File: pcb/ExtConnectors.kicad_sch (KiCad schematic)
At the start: 15 parts, among them J1 USB_C_Receptacle_USB2.0_14P, U2 TPD6S300ARUKR, U3 AP2112K-3.3

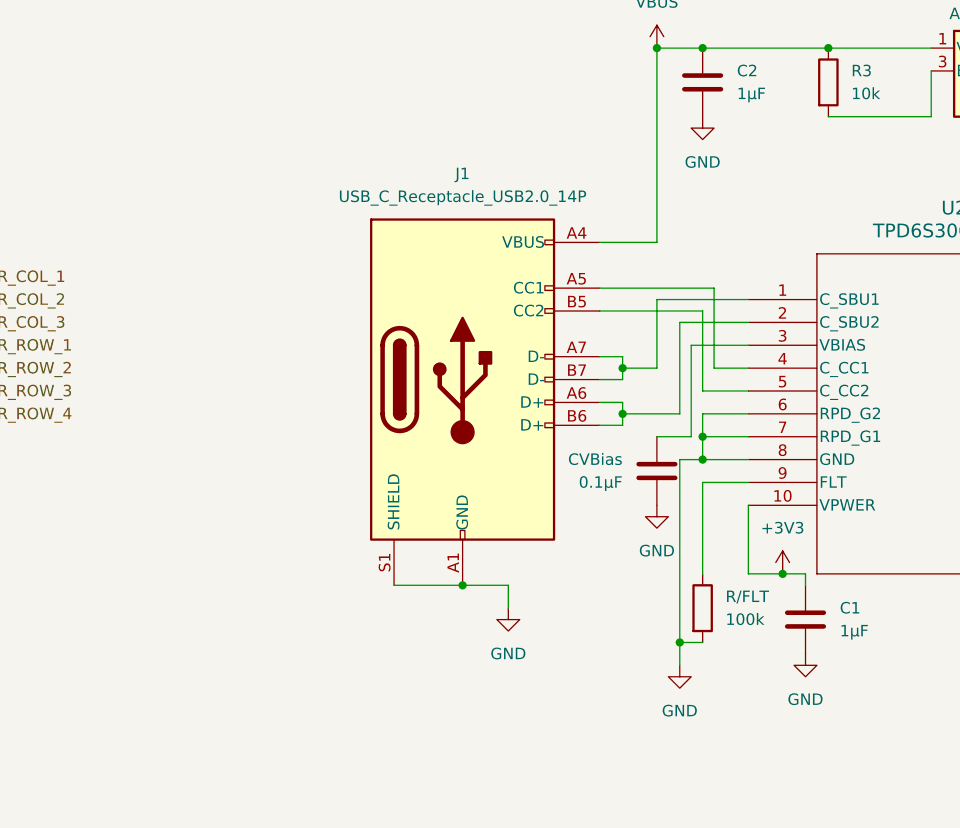
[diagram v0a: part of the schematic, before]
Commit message: First pass of applying footprints to most components.
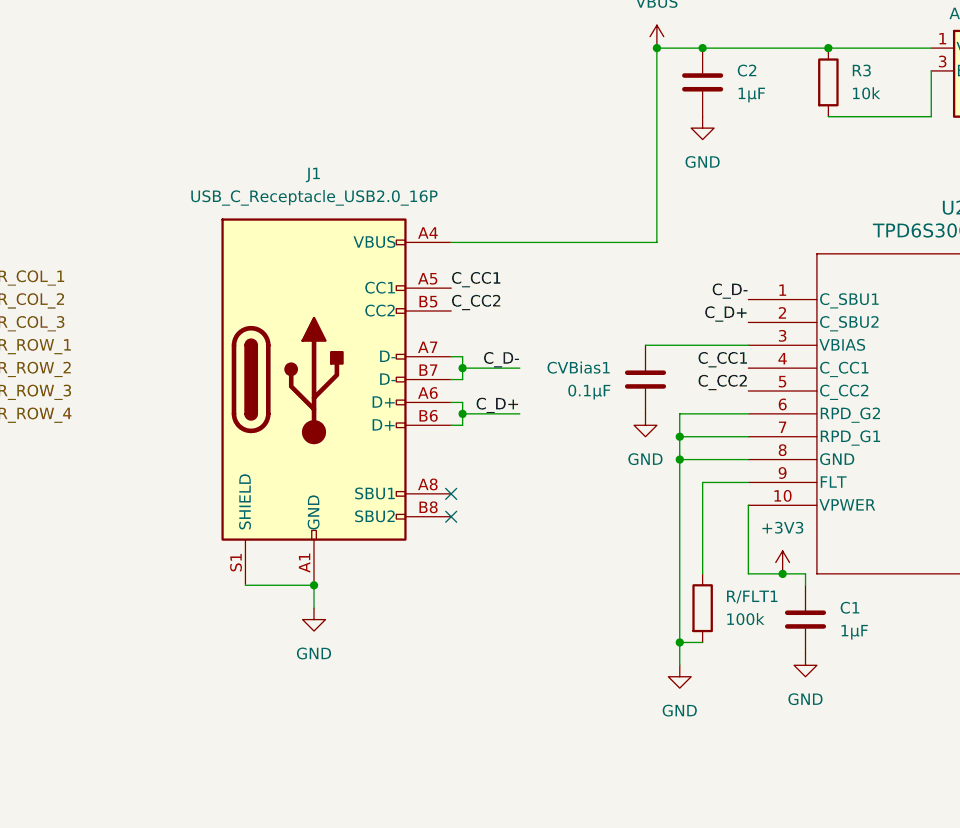
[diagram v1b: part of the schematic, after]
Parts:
- C1, C2, C3: footprint (none) -> Capacitor_SMD:C_0603_1608Metric_Pad1.08x0.95mm_HandSolder
- CVBias1: renamed from CVBias; footprint (none) -> Capacitor_SMD:C_0603_1608Metric_Pad1.08x0.95mm_HandSolder
- J1: value USB_C_Receptacle_USB2.0_14P -> USB_C_Receptacle_USB2.0_16P; symbol Connector:USB_C_Receptacle_USB2.0_14P -> Connector:USB_C_Receptacle_USB2.0_16P
- JP8, JP9: footprint (none) -> Jumper:SolderJumper-3_P1.3mm_Bridged12_RoundedPad1.0x1.5mm_NumberLabels
- R/FLT1: renamed from R/FLT; footprint (none) -> Resistor_SMD:R_0603_1608Metric_Pad0.98x0.95mm_HandSolder
- R1, R2, R3: footprint (none) -> Resistor_SMD:R_0603_1608Metric_Pad0.98x0.95mm_HandSolder
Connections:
- net C_CC1: now reaches J1.A5 (CC1), U2.4 (C_CC1)
- net C_D+: now reaches J1.A6 (D+), J1.B6 (D+), U2.2 (C_SBU2)
- net C_D-: now reaches J1.A7 (D-), J1.B7 (D-), U2.1 (C_SBU1)
- net C_CC2: now reaches J1.B5 (CC2), U2.5 (C_CC2)
- no-connect marks 0 -> 2
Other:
- moved on the sheet: CVBias1

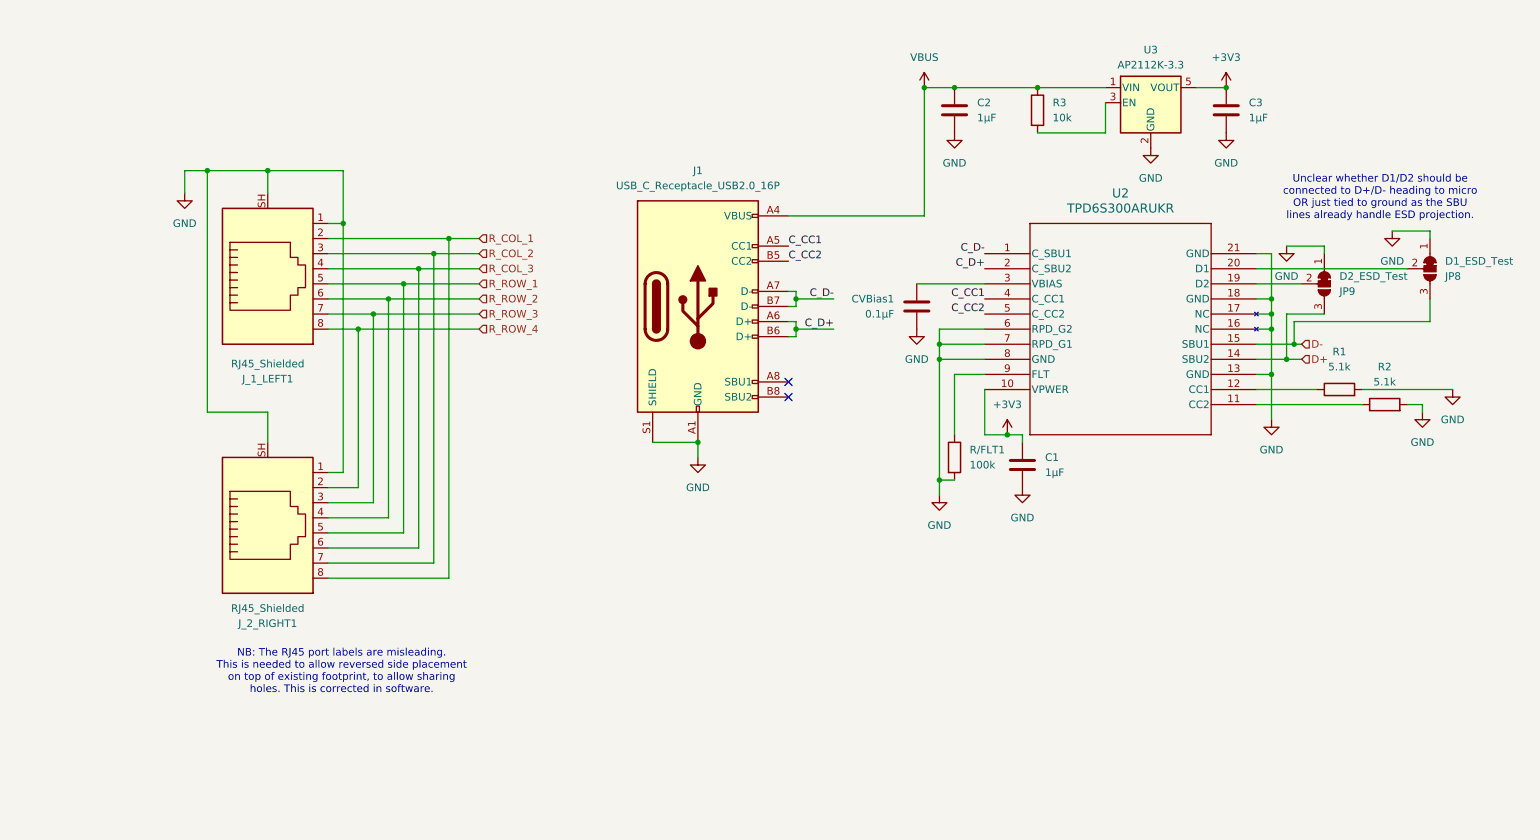
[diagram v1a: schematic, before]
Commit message: Switching from a full USB protection chip for OVP and ESD, needed for USB PD to only ESD protection. Also added chips for ESD protection for the Ethernet connectors to the other hand.
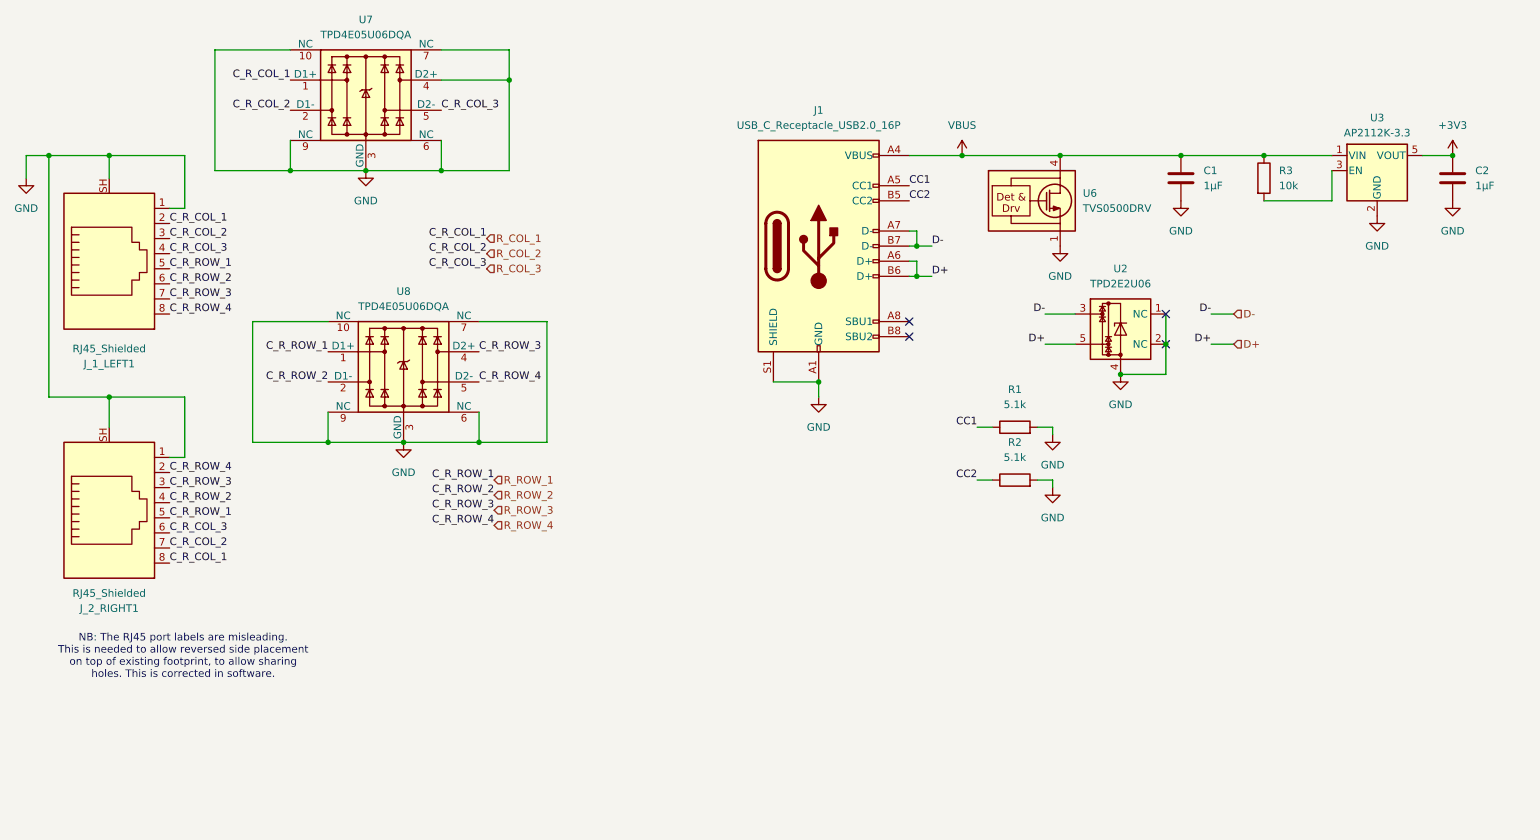
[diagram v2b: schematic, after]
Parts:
- removed C1: 1µF, Capacitor_SMD:C_0603_1608Metric_Pad1.08x0.95mm_HandSolder, symbol Device:C
- removed CVBias1: 0.1µF, Capacitor_SMD:C_0603_1608Metric_Pad1.08x0.95mm_HandSolder, symbol Device:C
- removed JP8: D1_ESD_Test, Jumper:SolderJumper-3_P1.3mm_Bridged12_RoundedPad1.0x1.5mm_NumberLabels, symbol Jumper:SolderJumper_3_Bridged12
- removed JP9: D2_ESD_Test, Jumper:SolderJumper-3_P1.3mm_Bridged12_RoundedPad1.0x1.5mm_NumberLabels, symbol Jumper:SolderJumper_3_Bridged12
- removed R/FLT1: 100k, Resistor_SMD:R_0603_1608Metric_Pad0.98x0.95mm_HandSolder, symbol Device:R
- removed U2: TPD6S300ARUKR, Extra:WQFN20_RUK_TEX, symbol Extra:TPD6S300ARUKR
- added U2: TPD2E2U06, Package_TO_SOT_SMD:SOT-543, symbol Power_Protection:TPD2E2U06
- added U6: TVS0500DRV, Package_SON:WSON-6-1EP_2x2mm_P0.65mm_EP1x1.6mm, symbol Power_Protection:TVS0500DRV
- added U7, U8: TPD4E05U06DQA, Package_SON:USON-10_2.5x1.0mm_P0.5mm, symbol Power_Protection:TPD4E05U06DQA
- renumbered C2 to C1, C3 to C2
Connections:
- net C_CC1 is gone; now on net CC1: J1.A5 (CC1)
- net C_CC2 is gone; now on net CC2: J1.B5 (CC2)
- net C_D+ is gone; now on net D+: J1.A6 (D+), J1.B6 (D+)
- net C_D- is gone; now on net D-: J1.A7 (D-), J1.B7 (D-)
- net D+: now also U2.5
- net D-: now also U2.3
- net GND: now also U2.1 (NC), U2.2 (NC), U2.4, U6.1 (GND), U6.2 (GND), U6.3 (GND), U6.7 (GND), U7.10 (NC), U7.3 (GND), U7.4 (D2+), U7.6 (NC), U7.7 (NC), U7.8 (GND), U7.9 (NC), U8.10 (NC), U8.3 (GND), U8.6 (NC), U8.7 (NC), U8.8 (GND), U8.9 (NC)
- net R_COL_1: now also U7.1 (D1+)
- net R_COL_2: now also U7.2 (D1-)
- net R_COL_3: now also U7.5 (D2-)
- net R_ROW_1: now also U8.1 (D1+)
- net R_ROW_2: now also U8.2 (D1-)
- net R_ROW_3: now also U8.4 (D2+)
- net R_ROW_4: now also U8.5 (D2-)
- net VBUS: now also U6.4 (IN), U6.5 (IN), U6.6 (IN)
- net CC1: now reaches R1.1
- net CC2: now reaches R2.1
- no-connect marks 2 -> 4
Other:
- note removed: "Unclear whether D1/D2 should be connected to D+/D- heading to micro OR just tied to ground as the SBU lines already handle ESD projection."
- moved on the sheet: C1, C2, J1, J_1_LEFT1, J_2_RIGHT1, R1, R2, R3, U3

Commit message: Updated all footprints and libraries to match planned components.
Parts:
- J1: footprint (none) -> Connector_USB:USB_C_Receptacle_GCT_USB4105-xx-A_16P_TopMnt_Horizontal
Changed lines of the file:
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@@
 			)
 		)
-		(property "Footprint" ""
+		(property "Footprint" "Connector_USB:USB_C_Receptacle_GCT_USB4105-xx-A_16P_TopMnt_Horizontal"
 			(at 161.29 63.5 0)
 			(effects

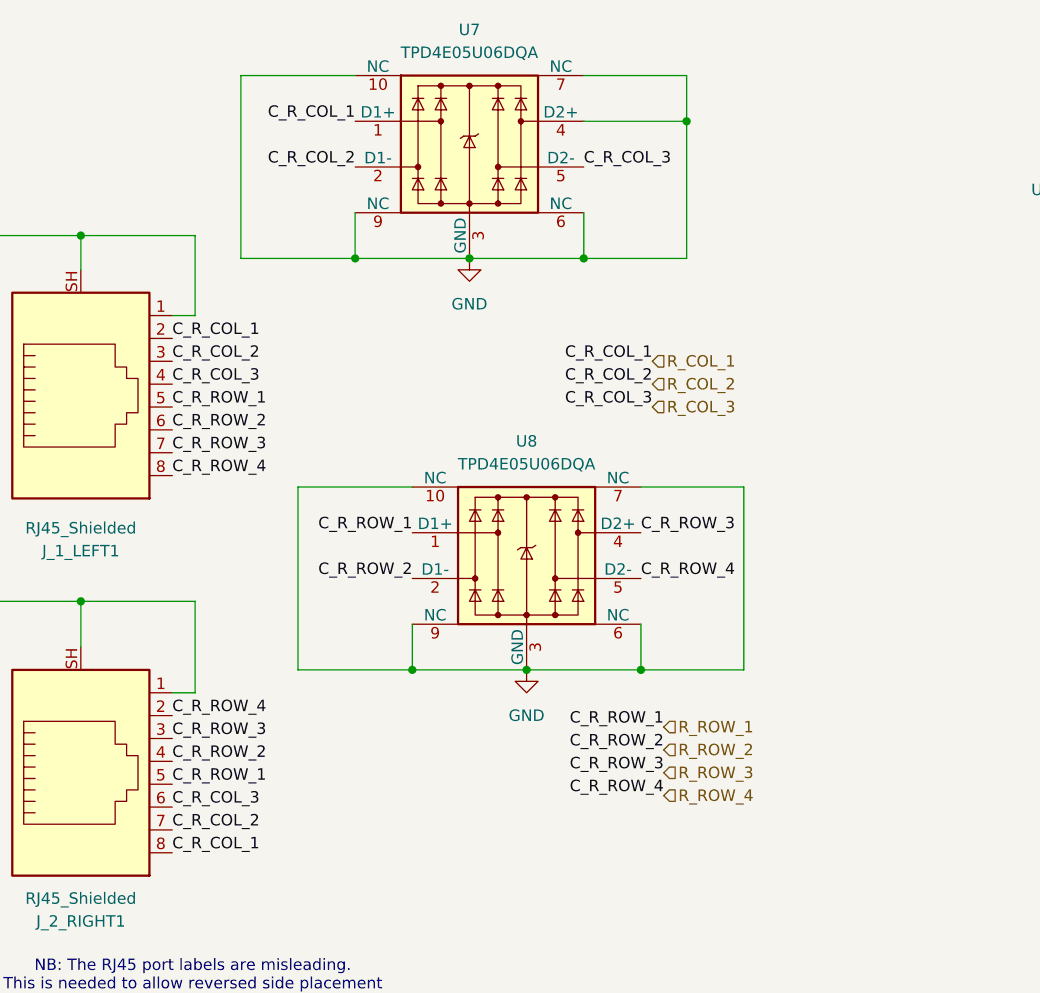
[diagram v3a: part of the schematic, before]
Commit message: Removed Rotary Encoder for space/flippability reasons and replaced all the key switch footprints that weren't bound properly to the schematic for some reason.
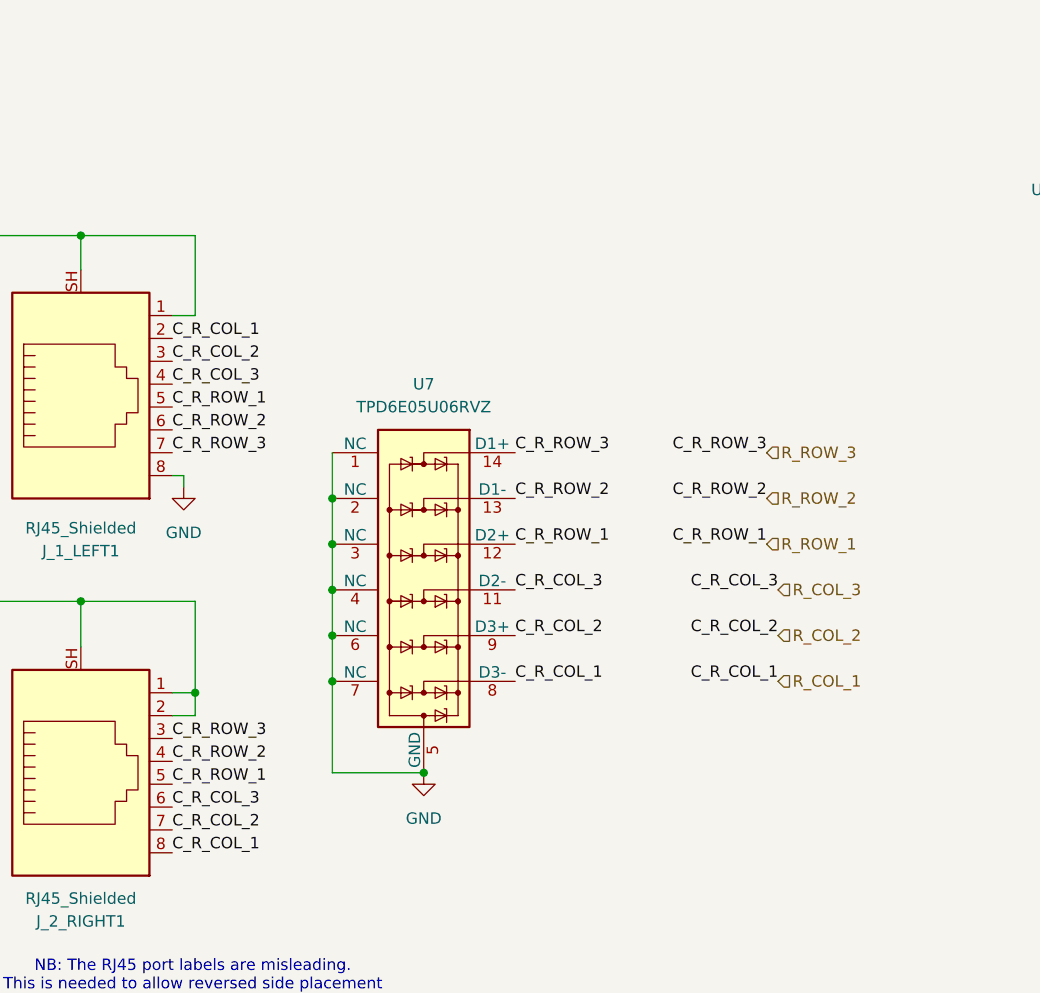
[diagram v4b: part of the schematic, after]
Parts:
- removed U7, U8: TPD4E05U06DQA, Package_SON:USON-10_2.5x1.0mm_P0.5mm, symbol Power_Protection:TPD4E05U06DQA
- added U7: TPD6E05U06RVZ, Package_SON:Texas_R-PUSON-N14, symbol Power_Protection:TPD6E05U06RVZ
- U2: footprint Package_TO_SOT_SMD:SOT-543 -> Package_TO_SOT_SMD:SOT-553
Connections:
- net R_ROW_4 is gone; now on net GND: J_1_LEFT1.8, J_2_RIGHT1.2
- net GND: now also U7.1 (NC), U7.10 (GND), U7.2 (NC), U7.3 (NC), U7.4 (NC), U7.5 (GND), U7.6 (NC), U7.7 (NC)
- net R_COL_1: now also U7.8 (D3-)
- net R_COL_2: now also U7.9 (D3+)
- net R_COL_3: now also U7.11 (D2-)
- net R_ROW_1: now also U7.12 (D2+)
- net R_ROW_2: now also U7.13 (D1-)
- net R_ROW_3: now also U7.14 (D1+)

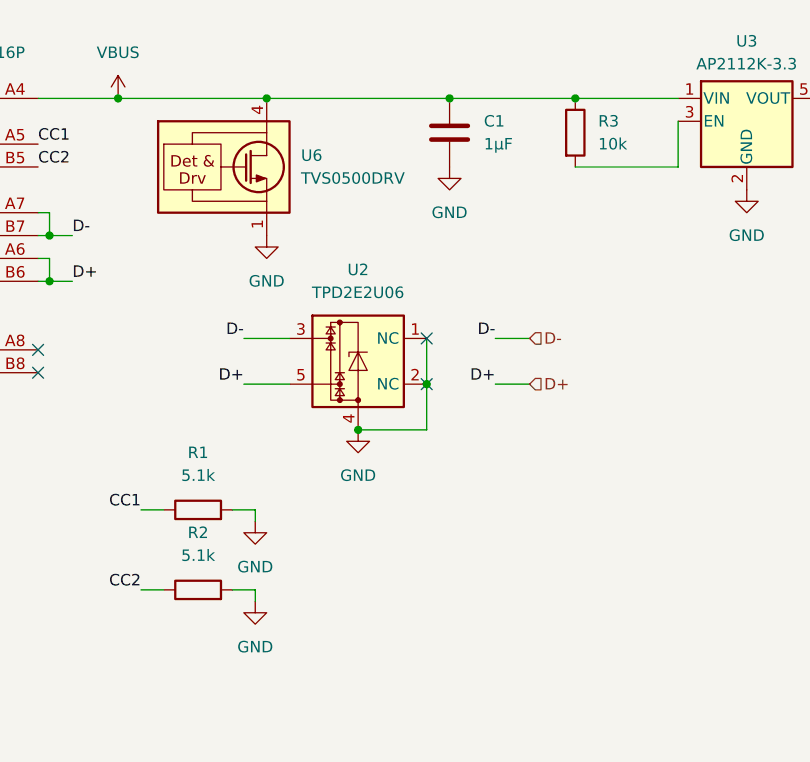
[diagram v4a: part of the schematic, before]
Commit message: Starting to position components and flipping passives as needed. Looking like board size is likely to need to be expanded.
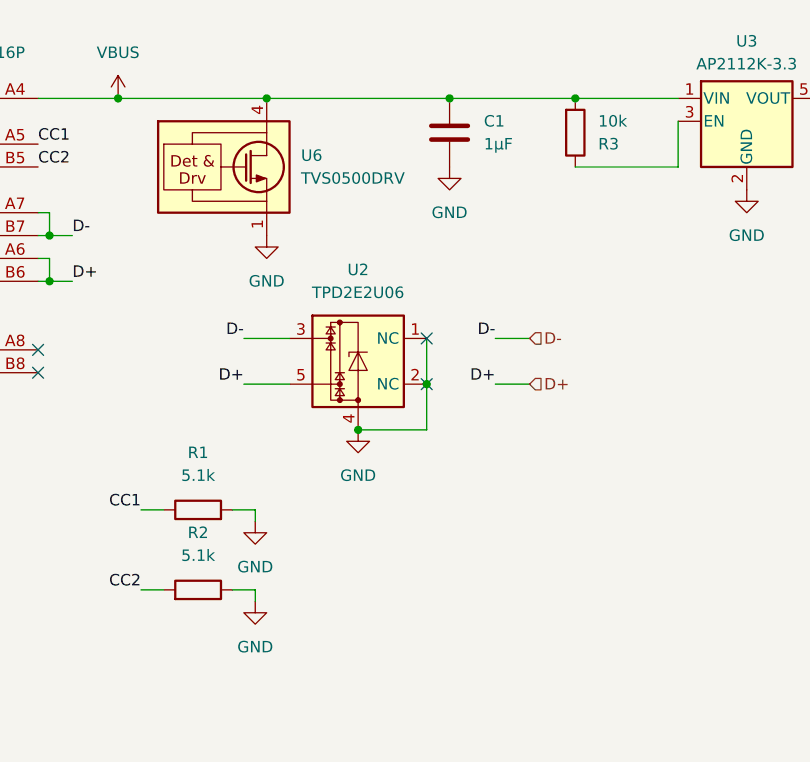
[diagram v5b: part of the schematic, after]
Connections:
- net CC2: now also R2.2; no longer R2.1
- net GND: now also R2.1; no longer R2.2
- net VBUS: now also R3.2; no longer R3.1
- net at U3.3 (EN): now also R3.1; no longer R3.2
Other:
- moved on the sheet: R2
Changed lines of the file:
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@@
 	(symbol
 		(lib_id "Device:R")
-		(at 190.5 102.87 90)
-		(unit 1)
-		(exclude_from_sim no)
-		(in_bom yes)
-		(on_board yes)
-		(dnp no)
-		(fields_autoplaced yes)
+		(at 190.5 102.87 270)
+		(mirror x)
+		(unit 1)
+		(exclude_from_sim no)
+		(in_bom yes)
+		(on_board yes)
+		(dnp no)
 		(property "Reference" "R2"
 			(at 190.5 96.52 90)
@@
 		(lib_id "Device:R")
 		(at 232.41 52.07 0)
+		(mirror x)
 		(unit 1)
 		(exclude_from_sim no)
@@
 		(dnp no)
 		(property "Reference" "R3"
-			(at 234.95 50.7999 0)
+			(at 234.95 53.3401 0)
 			(effects
 				(font
@@
 		)
 		(property "Value" "10k"
-			(at 234.95 53.3399 0)
-			(effects
-				(font
+			(at 234.95 50.8001 0)
+			(effects
+				(font
